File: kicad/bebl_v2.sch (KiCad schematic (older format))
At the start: 63 parts, among them P1 ISP, P2 FTDI, P3 LiPo, P4 USB-Micro, P5 Alt_Add, P6 Int1, P7 Int2, SW1 RST, U1 ATMEGA328, U2 FAN5346, U3 ADXL345, U4 MCP73831, U5 TPS61221DCK, X1 8MHz

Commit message: work in progress
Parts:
- B1, B10, B11, B12, B13, B2, B3, B4, B5, B6, B7, B8, B9: footprint (none) -> bebl_v2_pretty:breakout
- B14, B15: footprint (none) -> bebl_v2_pretty:batt_clip
- C1, C10, C11, C12, C13, C2, C3, C4, C5, C6, C7, C8, C9: footprint bebl_v2_legacy:c_0805 -> bebl_v2_pretty:c_0805
- D1, D2, D3, D4, D5, D6: footprint (none) -> bebl_v2_pretty:LED-5MM
- D7: footprint (none) -> bebl_v2_pretty:Diode-EMD2
- D8: footprint (none) -> bebl_v2_pretty:LED-0805
- L1: footprint (none) -> bebl_v2_pretty:Inductor_NLCV32
- L2: footprint (none) -> bebl_v2_pretty:Inductor_LQH3NPN
- P1: footprint ArthurC Lib:ISP -> bebl_v2_pretty:Header_3x2_ISP
- P2: footprint bebl_v2_legacy:PIN_ARRAY-6X1 -> bebl_v2_pretty:PIN_ARRAY-6X1
- P3: footprint bebl_v2_legacy:pin_strip_2 -> bebl_v2_pretty:CONN_JST-2_SMD
- P4: footprint ArthurC Lib:pin_strip_2 -> bebl_v2_pretty:USB_B_Micro
- P5, P6, P7: footprint (none) -> bebl_v2_pretty:solder_bridge_3
- R1, R2, R3, R4, R5, R6, R7: footprint bebl_v2_legacy:r_0805 -> bebl_v2_pretty:r_0805
- SC1, SC2, SC3, SC4: footprint bebl_v2_legacy:vite_3mm -> bebl_v2_pretty:screw_3mm
- SW1: footprint bebl_v2_legacy:Switch_SMT -> bebl_v2_pretty:Switch_SMT
- U1: footprint bebl_v2_legacy:TQFP32 -> bebl_v2_pretty:TQFP32
- U2: footprint (none) -> bebl_v2_pretty:SOT23-6
- U3: footprint (none) -> bebl_v2_pretty:ADXL345
- U4: footprint (none) -> bebl_v2_pretty:SOT23-5
- U5: footprint (none) -> bebl_v2_pretty:SOT23-6_LDO
- X1: footprint ArthurC Lib:Xtal_SMD4 -> bebl_v2_pretty:Xtal_SMD4
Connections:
- net GND: now also P4.T5, P4.T6

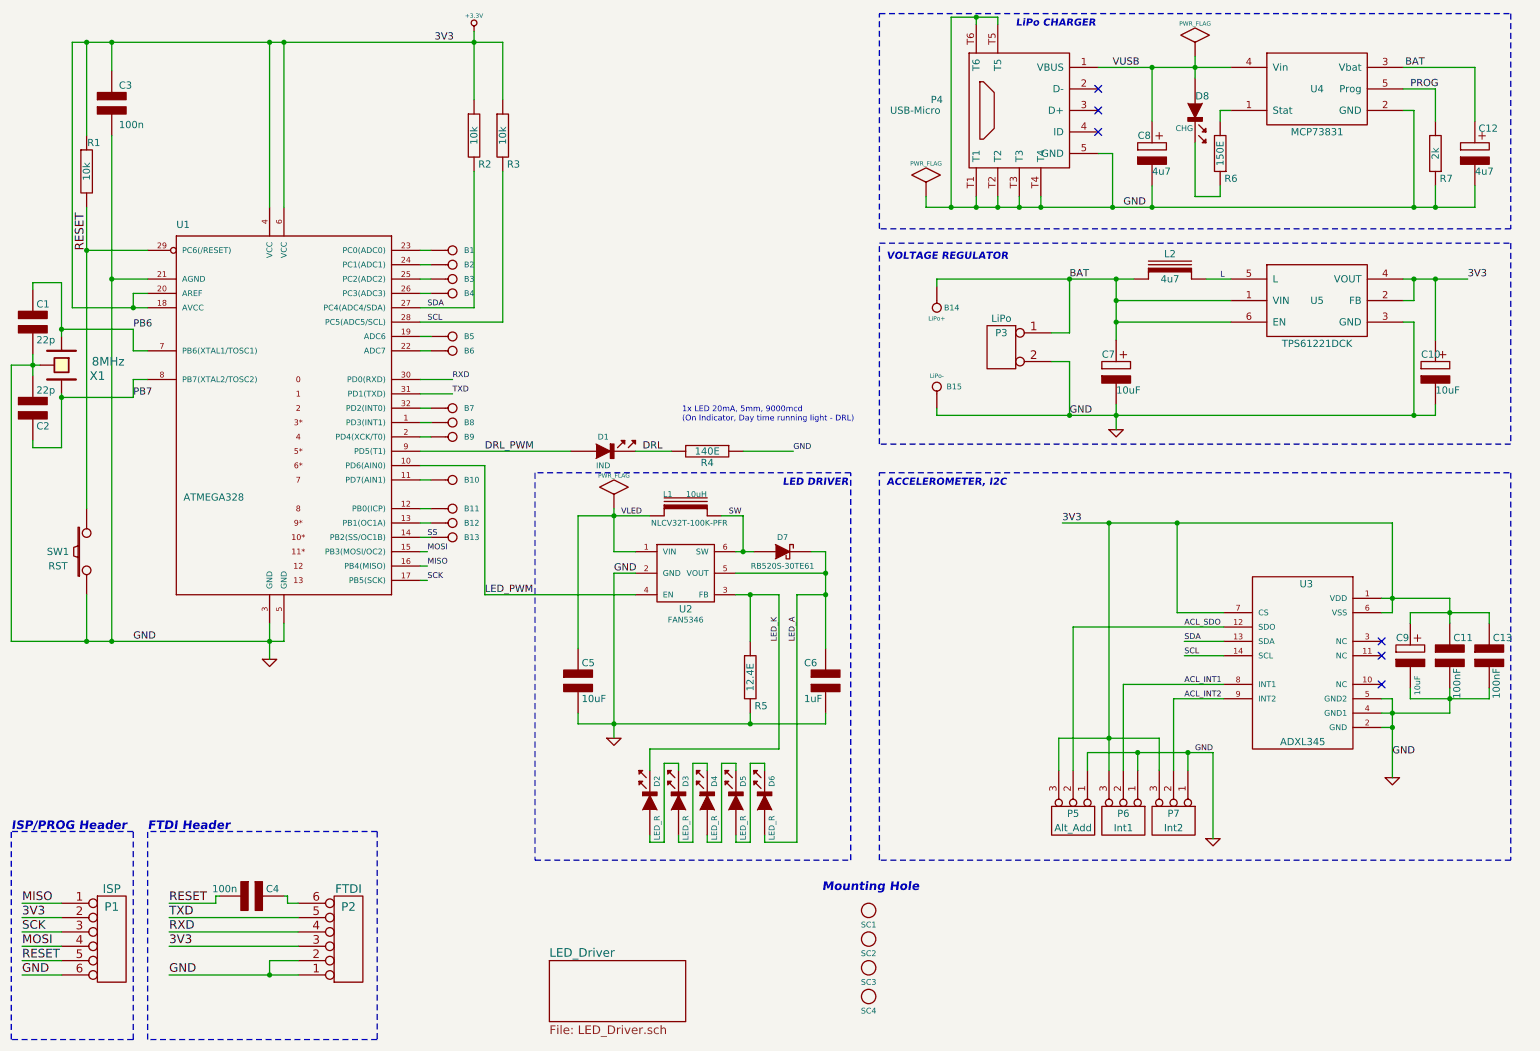
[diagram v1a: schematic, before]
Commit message: bebl_v2 3d mockup of 2 separate boards
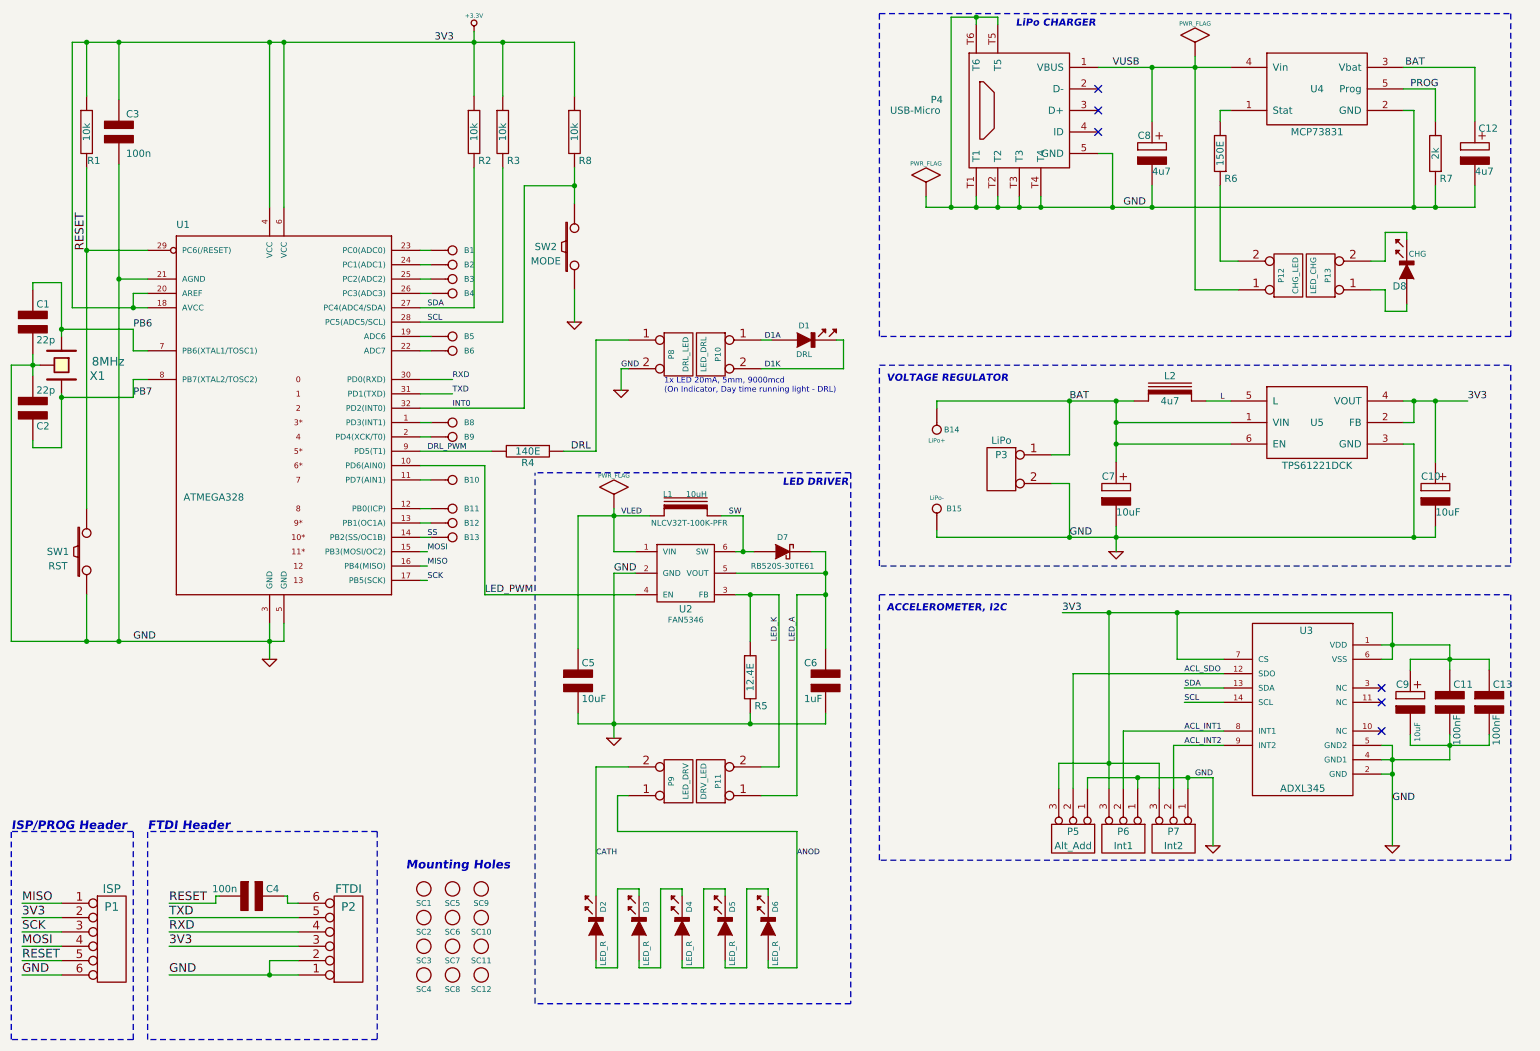
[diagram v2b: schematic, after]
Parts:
- removed B7: I/O, bebl_v2_pretty:breakout, symbol I/O
- added P10: LED_DRL, bebl_v2_pretty:pin_strip_2, symbol CONN_2
- added P11: DRV_LED, bebl_v2_pretty:pin_socket_2, symbol CONN_2
- added P12: CHG_LED, bebl_v2_pretty:pin_socket_2, symbol CONN_2
- added P13: LED_CHG, bebl_v2_pretty:pin_strip_2, symbol CONN_2
- added P8: DRL_LED, bebl_v2_pretty:pin_socket_2, symbol CONN_2
- added P9: LED_DRV, bebl_v2_pretty:pin_strip_2, symbol CONN_2
- added R8: 10k, bebl_v2_pretty:r_0805, symbol R
- added SC10, SC11, SC12, SC5, SC6, SC7, SC8, SC9: SCREW, bebl_v2_pretty:screw_3mm, symbol SCREW
- added SW2: MODE, bebl_v2_pretty:Switch_SMT, symbol SW_PUSH
- B1, B10, B11, B12, B13, B2, B3, B4, B5, B6, B8, B9: footprint bebl_v2_pretty:breakout -> bebl_v2_pretty:breakout_smd
- D1: value IND -> DRL
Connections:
- net +3.3V: now also R8.1
- net DRL: now also R4.1, P8.1 (P1); no longer D1.2 (K), R4.2
- net DRL_PWM: now also R4.2; no longer D1.1 (A)
- net GND: now also P8.2 (PM), SW2.1; no longer R4.1
- net LED_A: now also P11.1 (P1); no longer D6.1 (A)
- net LED_K: now also P11.2 (PM); no longer D2.2 (K)
- net VUSB: now also P12.1 (P1); no longer D8.1 (A)
- net INT0: now reaches U1.32 (PD2(INT0))
- net INT0: now also R8.2, SW2.2
- net at D8.2 (K): now also P13.2 (PM); no longer R6.1
- new net: D8.1 (A), P13.1 (P1)
- new net: P12.2 (PM), R6.1
- new net ANOD: D6.1 (A), P9.1 (P1)
- new net CATH: D2.2 (K), P9.2 (PM)
- new net D1A: D1.1 (A), P10.1 (P1)
- new net D1K: D1.2 (K), P10.2 (PM)
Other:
- note added: "Mounting Holes"
- note removed: "Mounting Hole"
- moved on the sheet: B14, B15, C10, C11, C13, C3, C7, C9, D1, D2, D3, D4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

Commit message: working on case for bebl_v2
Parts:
- removed B8, B9: I/O, bebl_v2_pretty:breakout_smd, symbol I/O
- removed P5: Alt_Add, bebl_v2_pretty:solder_bridge_3, symbol CONN_3
- removed P6: Int1, bebl_v2_pretty:solder_bridge_3, symbol CONN_3
- removed P7: Int2, bebl_v2_pretty:solder_bridge_3, symbol CONN_3
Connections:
- net ACL_SDO is gone; now on net GND: U3.12 (SDO)
- net ACL_INT1: now also U1.32 (PD2(INT0))
- net ACL_INT2: now also U1.1 (PD3(INT1))
- net MODE: now reaches U1.2 (PD4(XCK/T0))
- net MODE: now also R8.2, SW2.2
- removed net INT0: R8.2, SW2.2, U1.32 (PD2(INT0))
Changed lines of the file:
@@
 NoConn ~ 10100 5400
 Wire Wire Line
-	10175 5700 10175 6400
+	10175 5700 10175 6250
 Wire Wire Line
 	10100 5900 10175 5900
@@
 L GND #PWR04
 U 1 1 542E7DB5
-P 10175 6400
-F 0 "#PWR04" H 10175 6400 30  0001 C CNN
-F 1 "GND" H 10175 6330 30  0001 C CNN
-F 2 "" H 10175 6400 60  0001 C CNN
-F 3 "" H 10175 6400 60  0001 C CNN
-	1    10175 6400
+P 10175 6250
+F 0 "#PWR04" H 10175 6250 30  0001 C CNN
+F 1 "GND" H 10175 6180 30  0001 C CNN
+F 2 "" H 10175 6250 60  0001 C CNN
+F 3 "" H 10175 6250 60  0001 C CNN
+	1    10175 6250
 	1    0    0    -1
 $EndComp
@@
 	10575 5000 10575 5175
 Connection ~ 10575 5100
-Text Label 8725 5200 0    40   ~ 0
-ACL_SDO
-Wire Wire Line
-	8300 5600 9000 5600
-Wire Wire Line
-	8650 5700 9000 5700
+Wire Wire Line
+	8725 5600 9000 5600
+Wire Wire Line
+	8725 5700 9000 5700
 Wire Wire Line
 	9000 5400 8725 5400
@@
 	8725 5300 9000 5300
 Wire Wire Line
-	7950 5200 9000 5200
-Wire Wire Line
-	8675 5100 9000 5100
+	8625 5200 9000 5200
+Wire Wire Line
+	8625 5100 9000 5100
 Text Label 8725 5400 0    40   ~ 0
 SCL
@@
 ACL_INT2
 Wire Wire Line
-	7875 4775 10175 4775
-Wire Wire Line
-	8675 5100 8675 4775
-Connection ~ 8675 4775
-$Comp
-L CONN_3 P5
-U 1 1 542E7E0B
-P 7950 6350
-F 0 "P5" V 7900 6350 50  0000 C CNN
-F 1 "Alt_Add" V 8000 6350 50  0000 C CNN
-F 2 "bebl_v2_pretty:solder_bridge_3" H 7950 6350 60  0001 C CNN
-F 3 "" H 7950 6350 60  0000 C CNN
-F 4 "CONN HEADER 50POS .100\" SGL GOLD" H 7950 6450 60  0001 L CNN "Field4"
-F 5 "Header, Unshrouded, Male pin," H 7950 6550 60  0001 L CNN "Field5"
-F 6 "0.1\" pitch x 50 nos" H 7950 6650 60  0001 L CNN "Field6"
-F 7 "Samtec Inc" H 7950 6750 60  0001 L CNN "Field7"
-F 8 "TSW-150-07-L-S" H 7950 6850 60  0001 L CNN "Field8"
-F 9 "Digikey" H 7950 6950 60  0001 L CNN "Field9"
-F 10 "SAM1031-50-ND" H 7950 7050 60  0001 L CNN "Field10"
-F 11 "http://www.digikey.com/scripts/DkSearch/dksus.dll?WT.z_header=search_go&lang=en&keywords=SAM1031-50-ND&x=15&y=16&cur=USD" H 7950 7150 60  0001 L CNN "Field11"
-	1    7950 6350
-	0    1    1    0
-$EndComp
-$Comp
-L CONN_3 P6
-U 1 1 542E7E19
-P 8300 6350
-F 0 "P6" V 8250 6350 50  0000 C CNN
-F 1 "Int1" V 8350 6350 50  0000 C CNN
-F 2 "bebl_v2_pretty:solder_bridge_3" H 8300 6350 60  0001 C CNN
-F 3 "" H 8300 6350 60  0000 C CNN
-F 4 "CONN HEADER 50POS .100\" SGL GOLD" H 8300 6450 60  0001 L CNN "Field4"
-F 5 "Header, Unshrouded, Male pin," H 8300 6550 60  0001 L CNN "Field5"
-F 6 "0.1\" pitch x 50 nos" H 8300 6650 60  0001 L CNN "Field6"
-F 7 "Samtec Inc" H 8300 6750 60  0001 L CNN "Field7"
-F 8 "TSW-150-07-L-S" H 8300 6850 60  0001 L CNN "Field8"
-F 9 "Digikey" H 8300 6950 60  0001 L CNN "Field9"
-F 10 "SAM1031-50-ND" H 8300 7050 60  0001 L CNN "Field10"
-F 11 "http://www.digikey.com/scripts/DkSearch/dksus.dll?WT.z_header=search_go&lang=en&keywords=SAM1031-50-ND&x=15&y=16&cur=USD" H 8300 7150 60  0001 L CNN "Field11"
-	1    8300 6350
-	0    1    1    0
-$EndComp
-$Comp
-L CONN_3 P7
-U 1 1 542E7E27
-P 8650 6350
-F 0 "P7" V 8600 6350 50  0000 C CNN
-F 1 "Int2" V 8700 6350 50  0000 C CNN
-F 2 "bebl_v2_pretty:solder_bridge_3" H 8650 6350 60  0001 C CNN
-F 3 "" H 8650 6350 60  0000 C CNN
-F 4 "CONN HEADER 50POS .100\" SGL GOLD" H 8650 6450 60  0001 L CNN "Field4"
-F 5 "Header, Unshrouded, Male pin," H 8650 6550 60  0001 L CNN "Field5"
-F 6 "0.1\" pitch x 50 nos" H 8650 6650 60  0001 L CNN "Field6"
-F 7 "Samtec Inc" H 8650 6750 60  0001 L CNN "Field7"
-F 8 "TSW-150-07-L-S" H 8650 6850 60  0001 L CNN "Field8"
-F 9 "Digikey" H 8650 6950 60  0001 L CNN "Field9"
-F 10 "SAM1031-50-ND" H 8650 7050 60  0001 L CNN "Field10"
-F 11 "http://www.digikey.com/scripts/DkSearch/dksus.dll?WT.z_header=search_go&lang=en&keywords=SAM1031-50-ND&x=15&y=16&cur=USD" H 8650 7150 60  0001 L CNN "Field11"
-	1    8650 6350
-	0    1    1    0
-$EndComp
-Wire Wire Line
-	8650 6000 8650 5700
-Wire Wire Line
-	8300 5600 8300 6000
-Wire Wire Line
-	7950 6000 7950 5200
-Wire Wire Line
-	8550 5825 8550 6000
-Wire Wire Line
-	7850 5825 8550 5825
-Wire Wire Line
-	7850 5825 7850 6000
-Wire Wire Line
-	8200 4775 8200 6000
-Connection ~ 8200 5825
-Connection ~ 8200 4775
-Wire Wire Line
-	8050 6000 8050 5925
-Wire Wire Line
-	8050 5925 8925 5925
-Wire Wire Line
-	8750 5925 8750 6000
-Wire Wire Line
-	8400 6000 8400 5925
-Connection ~ 8400 5925
-Wire Wire Line
-	8925 5925 8925 6400
-Connection ~ 8750 5925
+	8400 4775 10175 4775
+Wire Wire Line
+	8625 5100 8625 4775
+Connection ~ 8625 4775
+Wire Wire Line
+	8625 6250 8625 5200
 $Comp
 L GND #PWR05
 U 1 1 542E7E3D
-P 8925 6400
-F 0 "#PWR05" H 8925 6400 30  0001 C CNN
-F 1 "GND" H 8925 6330 30  0001 C CNN
-F 2 "" H 8925 6400 60  0001 C CNN
-F 3 "" H 8925 6400 60  0001 C CNN
-	1    8925 6400
-	1    0    0    -1
-$EndComp
-Text Label 8925 5925 2    40   ~ 0
-GND
+P 8625 6250
+F 0 "#PWR05" H 8625 6250 30  0001 C CNN
+F 1 "GND" H 8625 6180 30  0001 C CNN
+F 2 "" H 8625 6250 60  0001 C CNN
+F 3 "" H 8625 6250 60  0001 C CNN
+	1    8625 6250
+	1    0    0    -1
+$EndComp
 Text Label 10175 6100 0    50   ~ 0
 GND
 Text Label 8725 5300 0    40   ~ 0
 SDA
-Text Label 7875 4775 0    50   ~ 0
+Text Label 8400 4775 0    50   ~ 0
 3V3
 $Comp
@@
 $EndComp
 $Comp
-L I/O B8
-U 1 1 54312216
-P 3625 3450
-F 0 "B8" H 3705 3450 40  0000 L CNN
-F 1 "I/O" H 3625 3505 30  0001 C CNN
-F 2 "bebl_v2_pretty:breakout_smd" H 3625 3450 60  0001 C CNN
-F 3 "" H 3625 3450 60  0000 C CNN
-	1    3625 3450
-	1    0    0    -1
-$EndComp
-$Comp
-L I/O B9
-U 1 1 5431222A
-P 3625 3550
-F 0 "B9" H 3705 3550 40  0000 L CNN
-F 1 "I/O" H 3625 3605 30  0001 C CNN
-F 2 "bebl_v2_pretty:breakout_smd" H 3625 3550 60  0001 C CNN
-F 3 "" H 3625 3550 60  0000 C CNN
-	1    3625 3550
-	1    0    0    -1
-$EndComp
-$Comp
 L I/O B10
 U 1 1 5431223E
@@
 Wire Wire Line
 	3475 4050 3400 4050
-Wire Wire Line
-	3400 3550 3475 3550
 Wire Wire Line
 	3400 3850 3475 3850
@@
 Text Notes 7550 700  0    50   Italic 10
 LiPo CHARGER
-Wire Wire Line
-	3400 3350 4125 3350
 Text Label 10300 1125 0    50   ~ 0
 PROG
@@
 Wire Wire Line
 	3400 3750 3850 3750
-Wire Wire Line
-	3475 3450 3400 3450
 Wire Wire Line
 	3400 3650 3900 3650
@@
 $EndComp
 Wire Wire Line
-	4125 3350 4125 1800
+	4125 1800 4125 3550
 Wire Wire Line
 	4125 1800 4475 1800
@@
 	1    0    0    -1
 $EndComp
-Text Label 3625 3350 0    40   ~ 0
-INT0
 Wire Wire Line
 	4625 3650 4625 2875
@@
 Wire Wire Line
 	8975 2325 9100 2325
+Wire Wire Line
+	4125 3550 3400 3550
+Wire Wire Line
+	3400 3350 3625 3350
+Wire Wire Line
+	3400 3450 3625 3450
+Text Label 3450 3550 0    40   ~ 0
+MODE
+Text Label 3625 3350 0    40   ~ 0
+ACL_INT1
+Text Label 3625 3450 0    40   ~ 0
+ACL_INT2
 $EndSCHEMATC

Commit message: bebl_v2 track layout, work in progress
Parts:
- removed SC10, SC11, SC12, SC9: SCREW, bebl_v2_pretty:screw_3mm, symbol SCREW
- P3: footprint bebl_v2_pretty:CONN_JST-2_SMD -> bebl_v2_pretty:pin_strip_2
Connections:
- net ACL_INT1: now also U1.1 (PD3(INT1)); no longer U1.32 (PD2(INT0))
- net ACL_INT2: now also U1.32 (PD2(INT0)); no longer U1.1 (PD3(INT1))
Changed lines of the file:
@@
 LIBS:power
 LIBS:bebl_v2-cache
-EELAYER 24 0
+EELAYER 25 0
 EELAYER END
 $Descr A4 11693 8268
@@
 F 0 "P3" H 7450 3875 50  0000 C CNN
 F 1 "LiPo" H 7450 3975 50  0000 C CNN
-F 2 "bebl_v2_pretty:CONN_JST-2_SMD" H 7450 3775 60  0001 C CNN
+F 2 "bebl_v2_pretty:pin_strip_2" H 7450 3775 60  0001 C CNN
 F 3 "" H 7450 3775 60  0001 C CNN
 	1    7450 3775
@@
 	1    0    0    -1
 $EndComp
-$Comp
-L SCREW SC9
-U 1 1 544E873B
-P 3825 6700
-F 0 "SC9" H 3825 6600 40  0000 C CNN
-F 1 "SCREW" H 3825 6800 40  0001 C CNN
-F 2 "bebl_v2_pretty:screw_3mm" H 3825 6700 60  0001 C CNN
-F 3 "" H 3825 6700 60  0001 C CNN
-	1    3825 6700
-	1    0    0    -1
-$EndComp
-$Comp
-L SCREW SC10
-U 1 1 544E8741
-P 3825 6900
-F 0 "SC10" H 3825 6800 40  0000 C CNN
-F 1 "SCREW" H 3825 7000 40  0001 C CNN
-F 2 "bebl_v2_pretty:screw_3mm" H 3825 6900 60  0001 C CNN
-F 3 "" H 3825 6900 60  0001 C CNN
-	1    3825 6900
-	1    0    0    -1
-$EndComp
-$Comp
-L SCREW SC11
-U 1 1 544E8747
-P 3825 7100
-F 0 "SC11" H 3825 7000 40  0000 C CNN
-F 1 "SCREW" H 3825 7200 40  0001 C CNN
-F 2 "bebl_v2_pretty:screw_3mm" H 3825 7100 60  0001 C CNN
-F 3 "" H 3825 7100 60  0001 C CNN
-	1    3825 7100
-	1    0    0    -1
-$EndComp
-$Comp
-L SCREW SC12
-U 1 1 544E874D
-P 3825 7300
-F 0 "SC12" H 3825 7200 40  0000 C CNN
-F 1 "SCREW" H 3825 7400 40  0001 C CNN
-F 2 "bebl_v2_pretty:screw_3mm" H 3825 7300 60  0001 C CNN
-F 3 "" H 3825 7300 60  0001 C CNN
-	1    3825 7300
-	1    0    0    -1
-$EndComp
 Wire Notes Line
 	11000 4650 11000 6500
@@
 Text Label 3450 3550 0    40   ~ 0
 MODE
+Text Label 3625 3450 0    40   ~ 0
+ACL_INT1
 Text Label 3625 3350 0    40   ~ 0
-ACL_INT1
-Text Label 3625 3450 0    40   ~ 0
 ACL_INT2
 $EndSCHEMATC

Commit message: working on case for bebl_v2
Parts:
- P3: value LiPo -> Ext_LiPo
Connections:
- net VLED is gone; now on net +3.3V: C5.1, L1.1, U2.1 (VIN)
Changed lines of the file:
@@
 LIBS:power
 LIBS:bebl_v2-cache
-EELAYER 25 0
+EELAYER 24 0
 EELAYER END
 $Descr A4 11693 8268
@@
 P 7450 3775
 F 0 "P3" H 7450 3875 50  0000 C CNN
-F 1 "LiPo" H 7450 3975 50  0000 C CNN
+F 1 "Ext_LiPo" H 7450 3975 50  0000 C CNN
 F 2 "bebl_v2_pretty:pin_strip_2" H 7450 3775 60  0001 C CNN
 F 3 "" H 7450 3775 60  0001 C CNN
@@
 	4750 4350 4900 4350
 Wire Wire Line
-	4750 4050 4750 4350
+	4750 4100 4750 4350
 Wire Wire Line
 	4500 4100 5000 4100
@@
 Text Label 5550 4100 0    40   ~ 0
 SW
-Text Label 4800 4100 0    40   ~ 0
-VLED
 $Comp
 L DIODE_LED D2
@@
 Wire Wire Line
 	5825 6700 5825 6750
-$Comp
-L PWR_FLAG #FLG09
-U 1 1 5448E6FF
-P 4750 4050
-F 0 "#FLG09" H 4750 4320 30  0001 C CNN
-F 1 "PWR_FLAG" H 4750 4280 30  0000 C CNN
-F 2 "" H 4750 4050 60  0000 C CNN
-F 3 "" H 4750 4050 60  0000 C CNN
-	1    4750 4050
-	1    0    0    -1
-$EndComp
 Text Label 3450 3650 0    40   ~ 0
 DRL_PWM
@@
 	4475 2525 4475 2750
 $Comp
-L GND #PWR010
+L GND #PWR09
 U 1 1 544ED2FD
 P 4475 2750
-F 0 "#PWR010" H 4475 2750 30  0001 C CNN
+F 0 "#PWR09" H 4475 2750 30  0001 C CNN
 F 1 "GND" H 4475 2680 30  0001 C CNN
 F 2 "" H 4475 2750 60  0001 C CNN
@@
 	4800 3075 4800 3225
 $Comp
-L GND #PWR011
+L GND #PWR010
 U 1 1 544F1460
 P 4800 3225
-F 0 "#PWR011" H 4800 3225 30  0001 C CNN
+F 0 "#PWR010" H 4800 3225 30  0001 C CNN
 F 1 "GND" H 4800 3155 30  0001 C CNN
 F 2 "" H 4800 3225 60  0001 C CNN
@@
 Text Label 3625 3350 0    40   ~ 0
 ACL_INT2
+Text Label 4500 4100 0    50   ~ 0
+3V3
 $EndSCHEMATC

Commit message: working on transistor based driver for leds
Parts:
- removed B11, B12, B13: I/O, bebl_v2_pretty:breakout_smd, symbol I/O
- removed C5: 10uF, bebl_v2_pretty:c_0805, symbol C_NPOL
- removed C6: 1uF, bebl_v2_pretty:c_0805, symbol C_NPOL
- removed D7: RB520S-30TE61, bebl_v2_pretty:Diode-EMD2, symbol DIODESCH
- removed L1: 10uH, bebl_v2_pretty:Inductor_NLCV32, symbol INDUCTOR2
- removed R4: 140E, bebl_v2_pretty:r_0805, symbol R
- removed R5: 12.4E, bebl_v2_pretty:r_0805, symbol R
- removed U2: FAN5346, bebl_v2_pretty:SOT23-6, symbol FAN5346
- added Q? (x6): BC847BDW1T1G, SOT-363, symbol BC847BDW1T1G
- added R? (x6): 56E, bebl_v2_pretty:r_0805, symbol R2
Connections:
- net labels removed: ANOD, CATH, D1A, D1K, DRL, DRL_PWM, LED_A, LED_K, LED_PWM, SW
- wire segments 224 -> 200
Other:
- note added: "1x LED 2.2V @ 20mA, 5mm, 9000mcd\n(On Indicator, Day time running light - DRL)"
- note removed: "1x LED 20mA, 5mm, 9000mcd\n(On Indicator, Day time running light - DRL)"
- moved on the sheet: B10, D1, D2, D3, D4, D5, D6, P10, P11, P8, P9
